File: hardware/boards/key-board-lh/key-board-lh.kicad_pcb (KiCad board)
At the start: 2 copper layers, 88.1 x 42 mm, 35 parts, among them J1 12-way, SW1 KS-33, SW2 KS-33, SW3 KS-33, SW4 KS-33, SW5 KS-33, U1 74HCS165

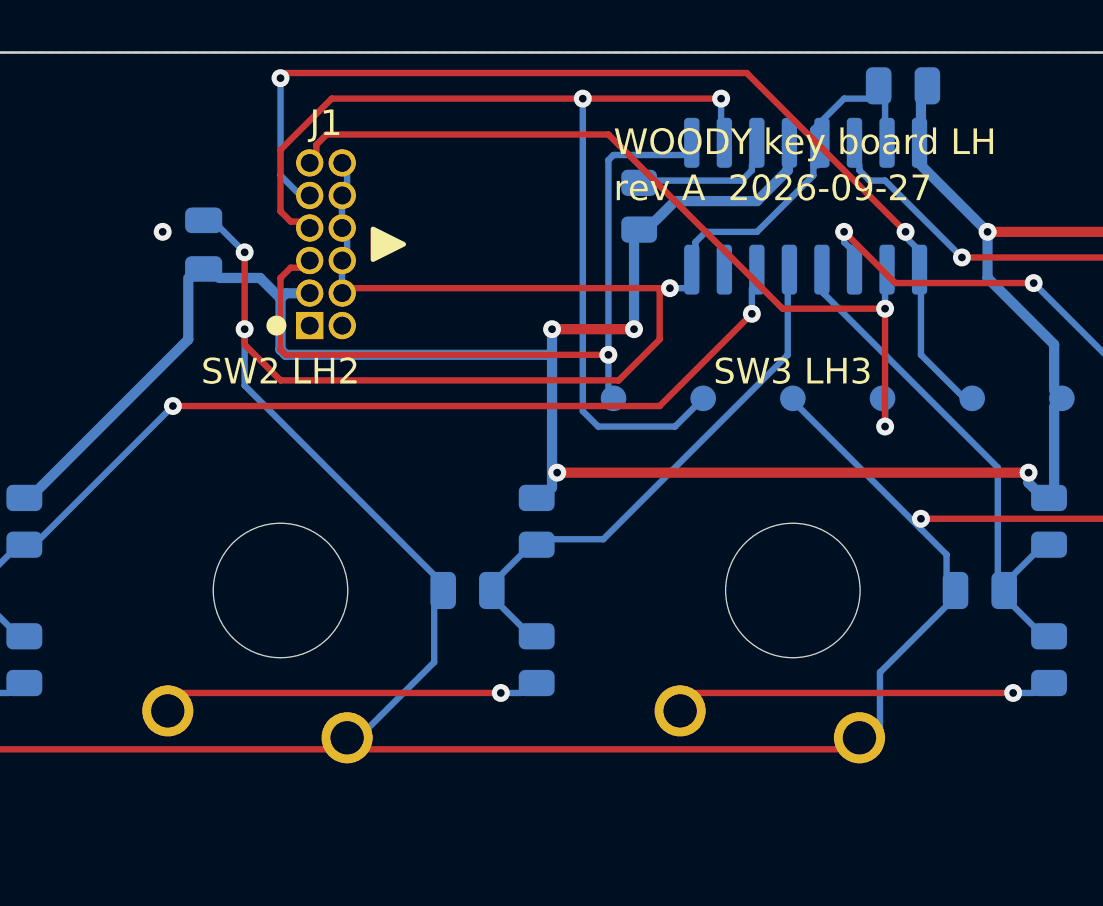
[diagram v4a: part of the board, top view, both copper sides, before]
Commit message: Lengthen J-CHAIN's pads on their free side
The 1.27 mm IDC header's pads were 1.07 round, which puts their ring
at JLC's 0.18 minimum. That ring can't grow where the pads face each
other: the pitch is 1.27 both ways, and the pin's diagonal sets the
drill. Each pad is now 1.50 long, extended away from the other row
with the hole offset in the copper. That gives 0.65 of ring on the
outer side, more copper against the ribbon's pull, and a connected
pad if the drill wanders into a thin side.

tools/pcb.py placed J-CHAIN's pin-1 dot and its top-side outline from
the hole positions. Both now measure from the pads' copper. The board
is re-laid, routed and re-rendered: pcb.py check reports 0 errors and
kicad.py check passes.

Co-Authored-By: Claude Opus 5.5 <noreply@anthropic.com>
Claude-Session: https://claude.ai/code/session_01LmB4muFXnoLprWX4JzuJ5A
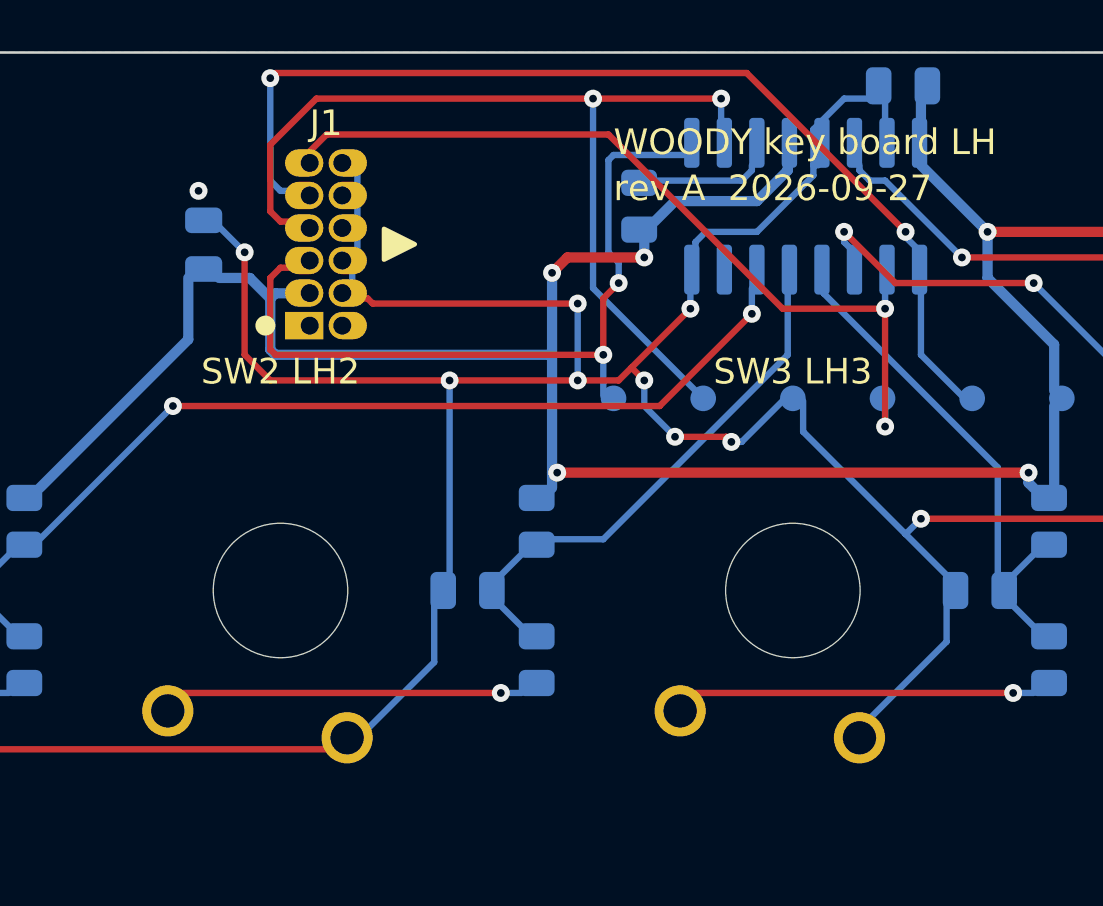
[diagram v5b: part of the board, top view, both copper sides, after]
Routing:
- net GND_CHAIN: track 166.1 -> 150.3 mm, vias 8 -> 13
- net /CHAIN_SER_LH: track 39.6 -> 36.0 mm
- net /HOP_LH_LT: track 28.9 -> 29.7 mm, vias 1 -> 2

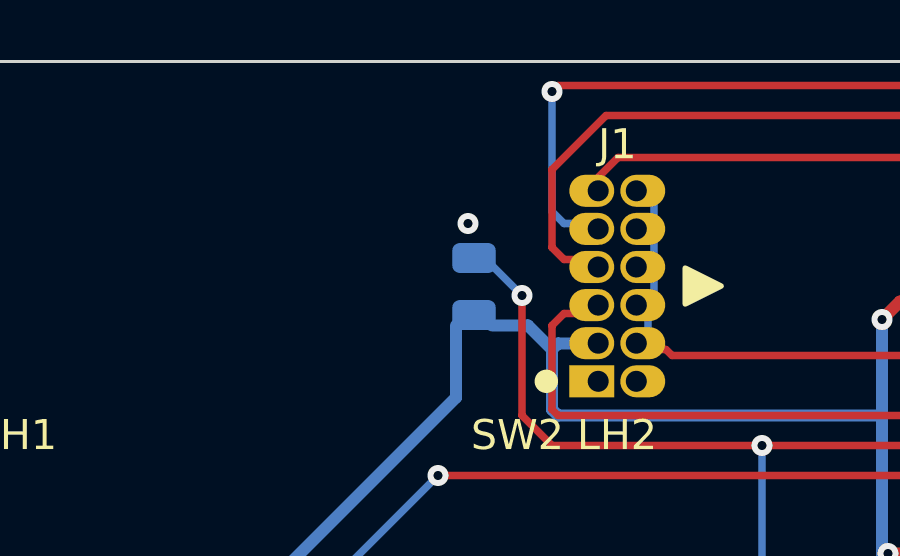
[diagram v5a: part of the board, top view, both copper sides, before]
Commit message: Fit C-BULK-CHAIN on both key boards instead of leaving it empty
The 10uF reservoir on each key board's 3V3 (C7 on the left-hand board,
C8 on the right) was a do-not-fit footprint, to be fitted at bring-up
only if the rail rang. It costs cents, so it is now a fitted,
machine-placed part (owner, 2026-09-28): Samsung CL21A106KAYNNNE, LCSC
C15850, a JLC Basic part.

The key-chain simulation now calls the fitted board "as ordered":
- rail-as-ordered: 5 mV peak to peak on the key board's 3V3.
- rail-impedance-as-ordered: a 2.2 ohm peak.
- The new rail-without-bulk holds the same limits with it left off
  (72 mV). A board built without the part still works; the part makes
  the rail quieter.
- rail-impedance-without-bulk (176-217 ohm peak) replaces
  rail-impedance-with-bulk; edge-droop-as-ordered is renamed
  edge-droop-decoupler-alone, since it models the decoupler with the
  bulk capacitor off.
Both boards' own simulations now include the part.

The sheets, the BOM row, the loom page, cluster-boards.md and both
board READMEs no longer treat it as optional. Both boards are re-laid
out (no DNP mark), checked at 0 errors and re-rendered, and the part
is in each board's JLC BOM and CPL.

Co-Authored-By: Claude Opus 5.5 <noreply@anthropic.com>
Claude-Session: https://claude.ai/code/session_01LmB4muFXnoLprWX4JzuJ5A
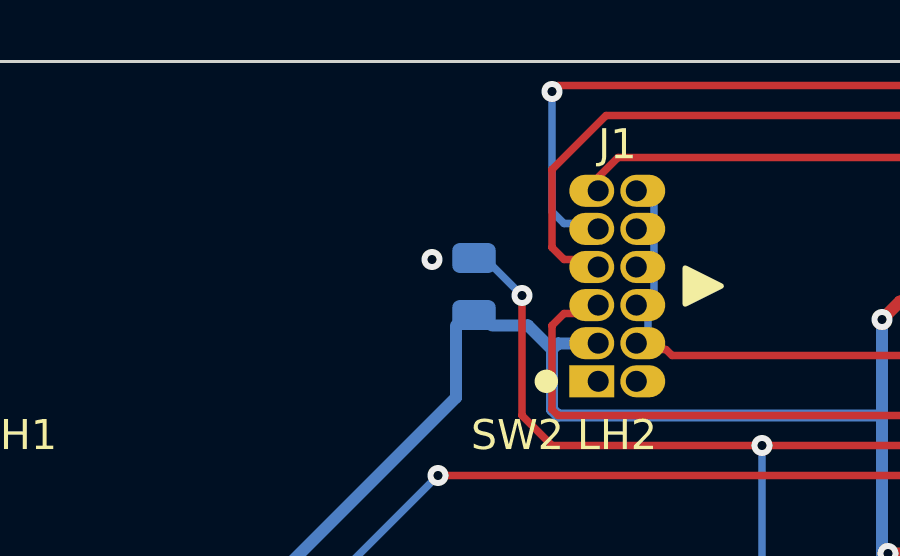
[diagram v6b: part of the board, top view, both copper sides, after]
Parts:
- C7: value 10uF DNP -> 10uF
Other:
- board text added: "C7"
- board text removed: "C7 DNP"

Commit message: Hang the key boards on PEM studs pressed flush into the plate
The owner asked for the key-board fasteners to be flush with the key
plate. A countersunk M2 head is as tall as the 1.20 mm plate is thick,
which would leave a knife-edge hole. So each corner now takes a PEM FHL
self-clinching flush-head stud pressed into the plate (owner:
"convert to that"). The rest of the stack is below the plate: spacer,
washer, the board, and a nut underneath. Nothing stands above the plate,
so the wood top has no pockets and there is no epoxy: the clinch keeps
each stud from turning, and the nuts still come off from below.

- M2.5: PEM's bulletin has no M2 flush-head stud. FHL rather than FH
  because PEM publishes FHL data in 1.2 mm aluminium (push-out 285 N,
  torque-out 0.55 N.m, nut torque 0.32 N.m) and it needs 2.8 mm to an
  edge. The model puts every stud 5.1 mm from the nearest cutout, where
  FH would need 5.4. Zinc-plated steel, per PEM's galvanic guidance.
  The bulletin and the finish guide are banked (R17).
- Spacer: no stocked M2.5 spacer is 1.8 mm, and 1.5 or 2.0 puts the
  board at the edge of the switch pins' window. Ettinger 005.52.023
  (2.0 mm) is faced down to 1.8 (banked, R18). The Wurth WA-SMST
  spacers carry a reflow spigot under the body, so the M2 one the old
  stack named was never a plain 2 mm spacer.
- body.yaml: kb_stud_* replace kb_screw_*, kb_pocket_* and
  kb_plate_hole. The washer and nut go to M2.5, and kb_mount_inset is
  now set by the nut's keep-out (3.6).
- New checks: stud edge distance, thread past the nut at the shortest
  stud, unthreaded shank inside the spacer, and the least tail margin
  (6.65 against the 10.1 kept). 0 clashes. The oak-pockets DXF is
  gone.
- Both key boards re-laid with M2.5 holes and keep-outs: 0 errors
  each, renders and fab regenerated.
- BOM: MECH-KB-STUD replaces MECH-KB-SCREW, the spacer, washer and nut
  rows go to M2.5, and ADH-EPOXY is removed.
- ADR 0020 Amendment 4 records the change. ADR 0009, cluster-boa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
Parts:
- H1, H2, H3, H4: value M2 mount -> mount; footprint MountingHole:MountingHole_2.2mm_M2 -> MountingHole:MountingHole_2.7mm_M2.5
- moved H1 0.28 mm to (100.6, 138.9)
- moved H2 0.28 mm to (100.6, 104.1)
- moved H3 0.28 mm to (181.5, 138.9)
- moved H4 0.28 mm to (181.5, 104.1)

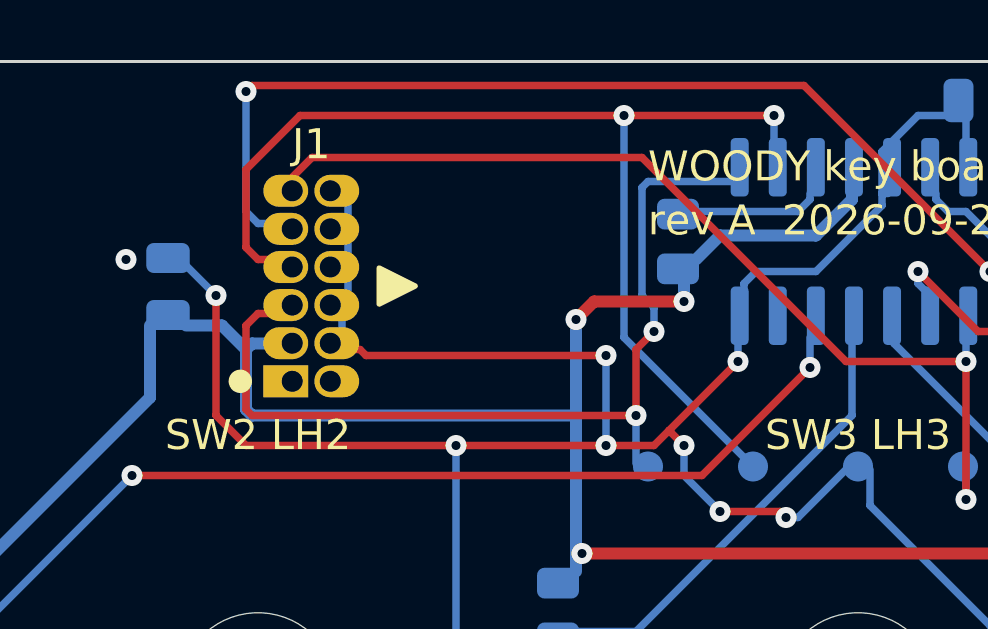
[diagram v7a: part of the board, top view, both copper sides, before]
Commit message: etherCON: PCB-mounted NE8FAV on an adapter, soldered to a main-board tongue (ADR 0021)
The instrument's etherCON becomes a Neutrik NE8FAV (A-series, vertical PCB,
rear mounting), soldered to a small adapter board behind the tail cap. J-UMB
becomes a 1 x 8 2.54 mm right-angle header soldered into the adapter and a
new tongue of the main board, so the umbilical has no cable and no mated
contact inside the body; CBL-UMB-PATCH is gone. Mounting the NE8FAH on the
main board directly would put its body 3 mm above the oak top's underside,
so the vertical part on an adapter it is. Latch up: the square flange
retires ADR 0009's rotation. The tail cap gets a recess from outside that
leaves the NE8FAV its 3 mm maximum panel.

- datasheets: NE8FAH, NE8FAH-C5 and NE8FAV drawings, data sheets and 3D
  models banked (fragment R23), with a BLOCKED row for the non-existent
  NE8FAH-C5E/-C6.
- config/body.yaml ethercon: NE8FAV numbers with sources; boards.umb_joint_*
  and umb_adapter_t; patch lead, rear socket and old J-UMB envelopes removed.
- CAD: the connector, adapter, J-UMB and tongue modelled; new DRC rules
  (adapter behind the Matrix, J-UMB under it, J-UMB's row clear of the
  footprint, the recess inside the face, the PUSH tab). 0 clashes.
- The patch plug no longer sets the tail: the body shortens by 1.9 mm, the
  hand gap drops to its minimum and the right hand moves 0.2 mm toward the
  mouth; the LH ribbon hairpin's clearance to the middle lid screw moved
  J-CHAIN LH 0.5 mm. Both key boards re-laid out from the body CAD (0
  errors each), renders and fab/ regenerated.
- BOM: J-UMBILICAL is the module end only; J-UMBILICAL-INST, PCB-UMB-ADAPTER
  and MECH-ETHERCON-SCREW added; J-UMB, PCB-CARRIER, ENDCAP-TAIL and the
  cable shell row updated (the NE8FAV does not name the NE8MX).
- spi-link netlist and circuit.yaml, carrier.md, spi-link.md, DESIGN.md,
  hardware/README.md, the register's body-thickness derivation, and pointers
  in ADRs 0001, 0004, 0009 and 0017. ADR inde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
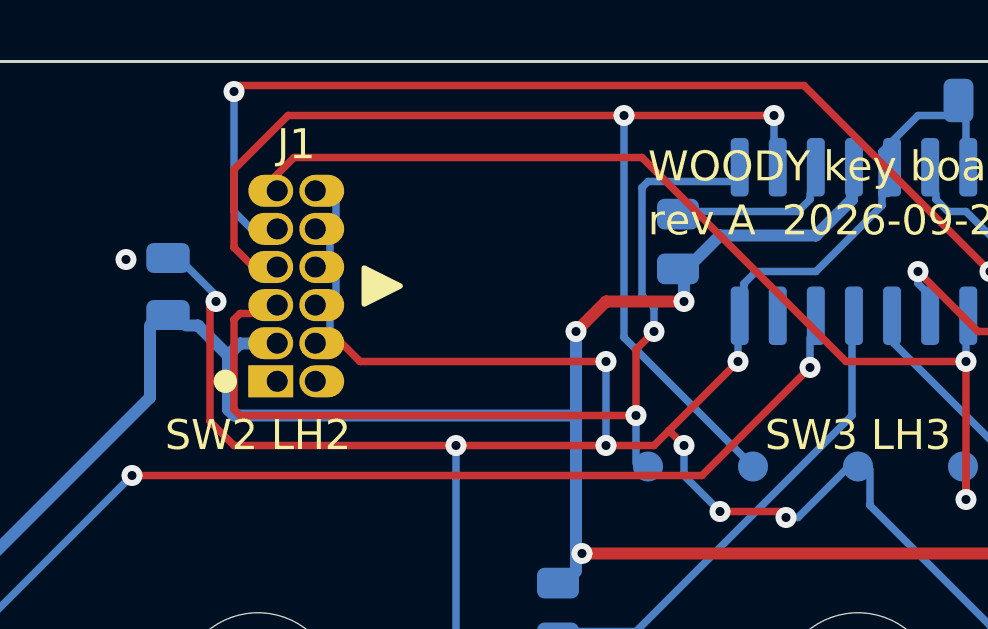
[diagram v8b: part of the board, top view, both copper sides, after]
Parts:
- moved J1 0.50 mm to (130.6, 111.2)
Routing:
- net GND_CHAIN: track 150.3 -> 151.1 mm
- net /CHAIN_SCK: track 31.9 -> 32.5 mm
- net /HOP_LH_LT: track 29.7 -> 30.3 mm
